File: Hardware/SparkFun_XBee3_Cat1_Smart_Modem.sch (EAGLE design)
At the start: 70 parts, among them J1 USB Female Type C Connector, J3 USB Female Type C Connector, J4 QWIIC_RIGHT_ANGLE, Q2 3.1A/30V/105mΩ, U1 FSUSB30MUX_MSOP10, U2 AP63203, U3 ESD Diode, U5 ESD Diode, U6 CP210X

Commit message: Fixes silk, aligns some text in the schematic, adds ordering instructions
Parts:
- added LOGO5: SPECIAL_INSTRUCTIONS-ORDERING, SparkFun-Aesthetics:SPECIAL_INSTRUCTIONS-ORDERING
- LOGO1: value SFE_LOGO_NAME.1_INCH -> SFE_LOGO_NAME.2_INCH; device SparkFun-Aesthetics:SFE_LOGO_NAME.1_INCH -> SparkFun-Aesthetics:SFE_LOGO_NAME.2_INCH
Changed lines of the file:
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@@
 <part name="PLED" library="SparkFun-Jumpers" deviceset="JUMPER-SMT_2_NC_TRACE" device="_SILK" package3d_urn="urn:adsk.eagle:package:39281/1"/>
 <part name="ALED" library="SparkFun-Jumpers" deviceset="JUMPER-SMT_2_NC_TRACE" device="_SILK" package3d_urn="urn:adsk.eagle:package:39281/1"/>
-<part name="LOGO1" library="SparkFun-Aesthetics" deviceset="SFE_LOGO_NAME" device=".1_INCH" value="SFE_LOGO_NAME.1_INCH"/>
 <part name="LOGO2" library="SparkFun-Aesthetics" deviceset="OSHW-LOGO" device="S"/>
 <part name="LOGO3" library="SparkFun-Aesthetics" deviceset="QWIIC_LOGO" device="_5MM" value="QWIIC_LOGO_5MM"/>
@@
 <part name="J10" library="SparkFun-Connectors" deviceset="CONN_01" device="PTH_NO_SILK_YES_STOP"/>
 <part name="SUPPLY13" library="SparkFun-PowerSymbols" deviceset="VIN" device=""/>
+<part name="LOGO1" library="SparkFun-Aesthetics" deviceset="SFE_LOGO_NAME" device=".2_INCH"/>
+<part name="LOGO5" library="SparkFun-Aesthetics" deviceset="SPECIAL_INSTRUCTIONS" device="-ORDERING"/>
 </parts>
 <sheets>
@@
 <text x="190.246" y="213.868" size="1.778" layer="97" font="vector">Cut SHLD/SHLD1 jumper to disconnect
 USB Shields from Ground. </text>
-<text x="177.8" y="99.06" size="2.54" layer="94" font="vector" align="center">Qwiic - I2C</text>
+<text x="172.72" y="101.6" size="2.54" layer="94" font="vector" align="center">Qwiic - I2C</text>
 <wire x1="0" y1="111.76" x2="121.92" y2="111.76" width="0.2032" layer="97" style="longdash"/>
 <wire x1="121.92" y1="111.76" x2="121.92" y2="187.96" width="0.2032" layer="97" style="longdash"/>
@@
 <text x="363.22" y="10.16" size="2.54" layer="94" font="vector" align="center">Elias Santistevan</text>
 <wire x1="223.52" y1="111.76" x2="223.52" y2="0" width="0.2032" layer="97" style="longdash"/>
-<text x="58.42" y="99.06" size="2.54" layer="94" font="vector" align="center">USB Switch - FSUSB30</text>
-<text x="58.42" y="91.44" size="1.778" layer="97" font="vector" align="center">Default (Low) = I2C (SDA)</text>
+<text x="58.42" y="101.6" size="2.54" layer="94" font="vector" align="center">USB Switch - FSUSB30</text>
+<text x="58.42" y="96.52" size="1.778" layer="97" font="vector" align="center">Default (Low) = I2C (SDA)</text>
 <wire x1="330.2" y1="111.76" x2="330.2" y2="35.56" width="0.2032" layer="97" style="longdash"/>
-<text x="281.94" y="99.06" size="2.54" layer="94" font="vector" align="center">Buttons and LEDs</text>
+<text x="274.32" y="101.6" size="2.54" layer="94" font="vector" align="center">Buttons and LEDs</text>
 <text x="195.58" y="187.96" size="1.778" layer="97" font="vector">VIN: 3.8 - 5.5V
 Iout: 2A Max</text>
 <text x="200.66" y="269.24" size="2.54" layer="94" font="vector" align="center">USB-C Connectors</text>
 <wire x1="121.92" y1="208.28" x2="294.64" y2="208.28" width="0.1524" layer="97" style="longdash"/>
-<text x="177.8" y="93.98" size="1.778" layer="97" font="vector" align="center">Cut I2C jumper to remove pullups.</text>
-<text x="281.94" y="93.98" size="1.778" layer="97" font="vector" align="center">Cut respective jumper to sever power to LED.</text>
+<text x="172.72" y="96.52" size="1.778" layer="97" font="vector" align="center">Cut I2C jumper to remove pullups.</text>
+<text x="274.32" y="96.52" size="1.778" layer="97" font="vector" align="center">Cut respective jumper to sever power to LED.</text>
 <text x="60.96" y="269.24" size="2.54" layer="94" font="vector" align="center">RF Module - XBee 3 Cat 1 Smart Modem</text>
 <wire x1="0" y1="187.96" x2="121.92" y2="187.96" width="0.2032" layer="97" style="longdash"/>
@@
 <attribute name="NAME" x="284.48" y="42.672" size="1.778" layer="95" font="vector" rot="R180" align="center"/>
 </instance>
-<instance part="LOGO1" gate="G$1" x="332.74" y="33.02" smashed="yes"/>
-<instance part="LOGO2" gate="G$1" x="401.32" y="45.72" smashed="yes"/>
-<instance part="LOGO3" gate="G$1" x="421.64" y="40.64" smashed="yes"/>
+<instance part="LOGO2" gate="G$1" x="401.32" y="48.26" smashed="yes"/>
+<instance part="LOGO3" gate="G$1" x="421.64" y="48.26" smashed="yes"/>
 <instance part="U2" gate="G$1" x="231.14" y="142.24" smashed="yes">
 <attribute name="NAME" x="223.52" y="150.368" size="1.778" layer="95" font="vector"/>
@@
 <attribute name="VALUE" x="45.72" y="172.974" size="1.778" layer="96" font="vector" align="bottom-center"/>
 </instance>
+<instance part="LOGO1" gate="G$1" x="330.2" y="35.56" smashed="yes"/>
+<instance part="LOGO5" gate="G$1" x="431.8" y="35.56" smashed="yes" rot="MR0"/>
 </instances>
 <busses>

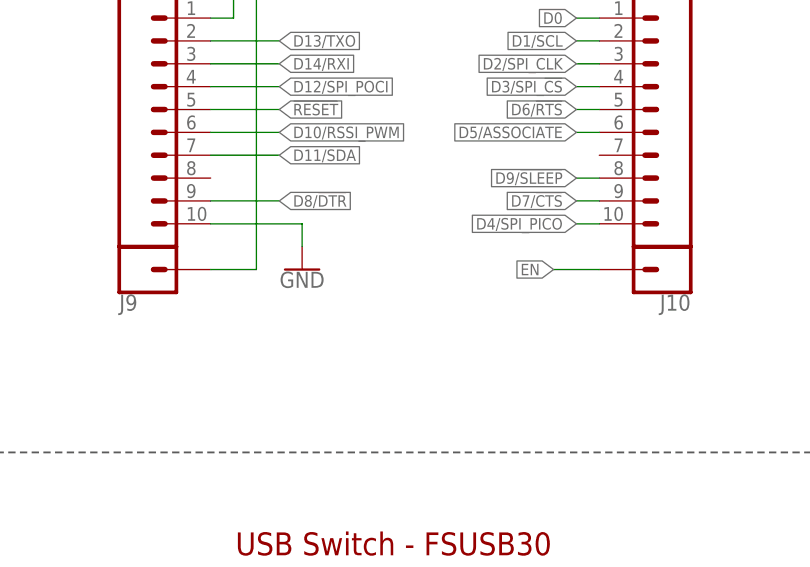
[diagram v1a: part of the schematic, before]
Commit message: Updates single PTH with new footprint
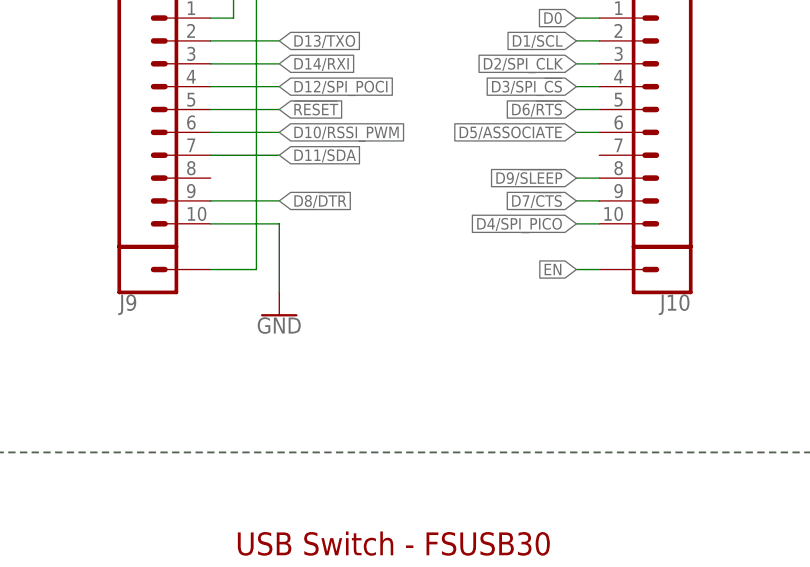
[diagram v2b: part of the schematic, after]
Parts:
- J10, J9: device SparkFun-Connectors:CONN_01PTH_NO_SILK_YES_STOP -> SparkFun-Connectors:CONN_01PTH_NO_SILK_STAND
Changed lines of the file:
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@@
 <part name="R4" library="SparkFun-Resistors" deviceset="10KOHM" device="-0603-1/10W-1%" value="10k"/>
 <part name="SUPPLY6" library="SparkFun-PowerSymbols" deviceset="3.3V" device=""/>
-<part name="J9" library="SparkFun-Connectors" deviceset="CONN_01" device="PTH_NO_SILK_YES_STOP"/>
-<part name="J10" library="SparkFun-Connectors" deviceset="CONN_01" device="PTH_NO_SILK_YES_STOP"/>
+<part name="J9" library="SparkFun-Connectors" deviceset="CONN_01" device="PTH_NO_SILK_STAND"/>
+<part name="J10" library="SparkFun-Connectors" deviceset="CONN_01" device="PTH_NO_SILK_STAND"/>
 <part name="SUPPLY13" library="SparkFun-PowerSymbols" deviceset="VIN" device=""/>
 <part name="LOGO1" library="SparkFun-Aesthetics" deviceset="SFE_LOGO_NAME" device=".2_INCH"/>
@@
 <attribute name="VALUE" x="40.64" y="172.974" size="1.778" layer="96" font="vector" align="bottom-center"/>
 </instance>
-<instance part="GND17" gate="1" x="48.26" y="132.08" smashed="yes" rot="MR0">
-<attribute name="VALUE" x="48.26" y="131.826" size="1.778" layer="96" font="vector" rot="MR0" align="top-center"/>
+<instance part="GND17" gate="1" x="45.72" y="127" smashed="yes" rot="MR0">
+<attribute name="VALUE" x="45.72" y="126.746" size="1.778" layer="96" font="vector" rot="MR0" align="top-center"/>
 </instance>
 <instance part="R4" gate="G$1" x="238.76" y="63.5" smashed="yes" rot="R90">
@@
 </segment>
 <segment>
-<wire x1="48.26" y1="137.16" x2="48.26" y2="134.62" width="0.1524" layer="91"/>
+<wire x1="45.72" y1="137.16" x2="45.72" y2="129.54" width="0.1524" layer="91"/>
 <pinref part="GND17" gate="1" pin="GND"/>
 <pinref part="J6" gate="J1" pin="10"/>
-<wire x1="48.26" y1="137.16" x2="38.1" y2="137.16" width="0.1524" layer="91"/>
+<wire x1="45.72" y1="137.16" x2="38.1" y2="137.16" width="0.1524" layer="91"/>
 </segment>
 </net>
@@
 </segment>
 <segment>
-<wire x1="76.2" y1="132.08" x2="81.28" y2="132.08" width="0.1524" layer="91"/>
-<label x="76.2" y="132.08" size="1.27" layer="95" font="vector" rot="MR0" xref="yes"/>
+<wire x1="78.74" y1="132.08" x2="81.28" y2="132.08" width="0.1524" layer="91"/>
+<label x="78.74" y="132.08" size="1.27" layer="95" font="vector" rot="MR0" xref="yes"/>
 <pinref part="J10" gate="G$1" pin="1"/>
 </segment>

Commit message: Updates design to use the FT231XS instead of the CP2102N
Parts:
- removed C8: 4.7uF, SparkFun-Capacitors:4.7UF-0603-6.3V-(10%)
- removed R17: 22k, SparkFun-Resistors:22KOHM-0603-1/10W-1%
- removed R18: 33k, SparkFun-Resistors:33KOHM-0603-1/10W-1%
- removed R4, R9: 10k, SparkFun-Resistors:10KOHM-0603-1/10W-1%
- removed U6: CP210X, SparkFun-IC-Comms:CP2102N
- added C11, C14: 0.1uF, SparkFun-Capacitors:0.1UF-0603-25V-(+80/-20%)
- added C12: 10pF, SparkFun-Capacitors:10PF-0603-50V-5%
- added C13: 47pF, SparkFun-Capacitors:47PF-0603-50V-5%
- added R5: 100, SparkFun-Resistors:100OHM-0603-1/10W-1%
- added U7: FT231XS, SparkFun-IC-Comms:FT231XS
- D4: value BLUE -> Yellow; device SparkFun-LED:LED-BLUE0603 -> SparkFun-LED:LED-YELLOW0603
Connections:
- removed net N$10: R17.1, R18.2, U6.VBUS
- removed net N$9: R9.2, U6.!RSTB
- new net N$3: R5.1, U1.VCC
- net !RESET!: no longer R4.1
- net 3.3V: now also C11.1, C12.1, C13.1, C14.1, R5.2; no longer C8.1, R4.2, R9.1, U1.VCC, U6.VDD, U6.VIO, U6.VREGIN
- net D+: now also U7.USBDP; no longer U6.D+
- net D-: now also U7.USBDM; no longer U6.D-
- net D13/TXO: now also U7.RXD; no longer U6.RXD
- net D14/RXI: now also U7.TXD; no longer U6.TXD
- net D6/!RTS!: now also U7.!RTS; no longer U6.RTS
- net D7/!CTS!: now also U7.!CTS; no longer U6.CTS
- net D8/!DTR!: now also U7.!DTR; no longer U6.DTR
- net GND: now also C11.2, C12.2, C13.2, C14.2, U7.!RESET, U7.3V3OUT, U7.GND@16, U7.GND@6, U7.VCC, U7.VCCIO; no longer C8.2, R18.1, U6.GND
- net VIN: no longer R17.2
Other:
- note added: "USB to UART Bridge - FT231XS"
- note removed: "USB to UART Bridge - CP2104/2N"
- moved on the sheet: C10, C5, C6, C7, C9, J2
